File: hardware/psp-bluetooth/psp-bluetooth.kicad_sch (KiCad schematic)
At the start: 16 parts, among them J1 Left Connector, J2 Center Connector, J3 Right Connector, J4 Analog Connector, J5 PSP Power out, J6 Power IN, J7 Serial, J8 Vin Toggle, P1 Digital, P2 Analog, P3 CONN_01X01, P4 CONN_01X01, P5 CONN_01X01, P6 CONN_01X01, U1 MCP4251-xxxx-P

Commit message: Final
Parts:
- removed J6: Power IN, Connector_PinHeader_2.54mm:PinHeader_1x02_P2.54mm_Vertical, symbol Connector_Generic:Conn_01x02
- added J6: Barrel_Jack, Connector_BarrelJack:BarrelJack_CUI_PJ-063AH_Horizontal, symbol Connector:Barrel_Jack
- added JP1: SJ Vin Toggle, Jumper:SolderJumper-2_P1.3mm_Open_Pad1.0x1.5mm, symbol Jumper:SolderJumper_2_Open
- added SW1: SW_Push, Button_Switch_SMD:SW_Push_1P1T_NO_6x6mm_H9.5mm, symbol Switch:SW_Push
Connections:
- net 10(**/SS): no longer U1.1 (~{CS})
- net 11(**/MOSI): no longer U1.3 (SDI)
- net A6 (D20): now also SW1.1
- net GND: now also J6.1, SW1.2
- net VIN: now also JP1.2 (B)
- net P1W: now reaches J4.2 (Pin_2), U1.6 (P1W)
- net P0A/P1A: now reaches J4.3 (Pin_3), U1.7 (P1A), U1.8 (P0A)
- net P0W: now reaches J4.4 (Pin_4), U1.9 (P0W)
- net at J5.2 (Pin_2), J8.1 (Pin_1), S1.2: now also JP1.1 (A)
- net at S1.3: now also J6.2
- new net 10(**/SS): U1.1 (~{CS})
- new net 11(**/MOSI): U1.3 (SDI)
- no-connect marks 18 -> 17
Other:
- moved on the sheet: J7

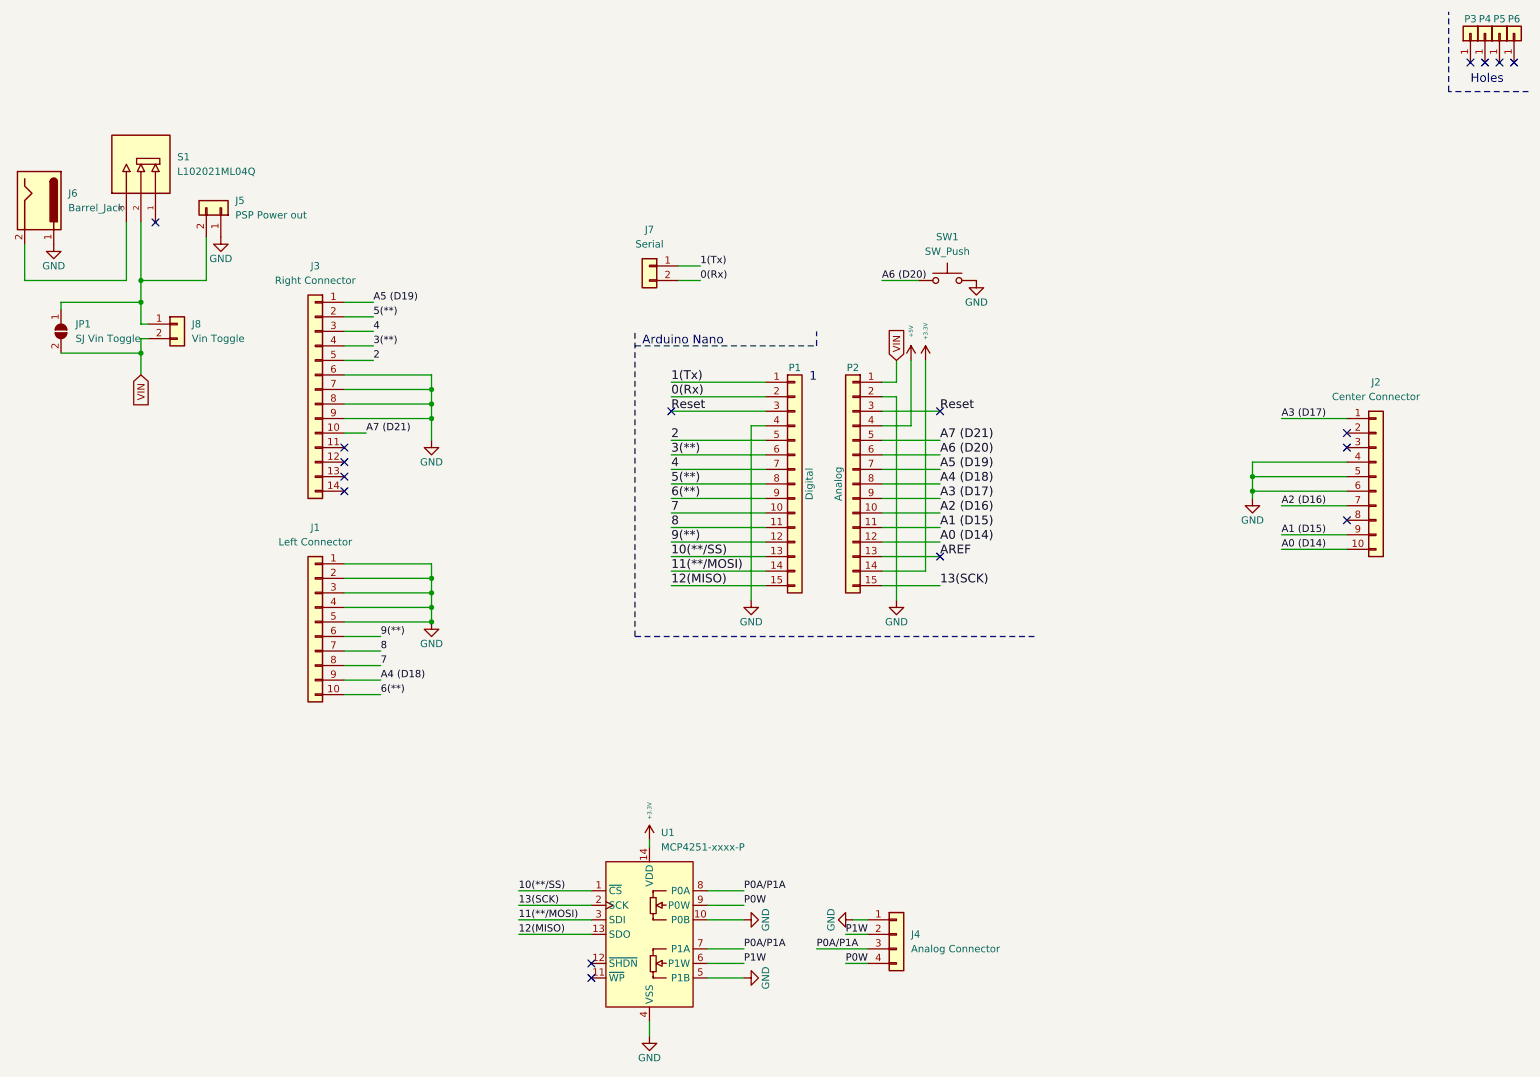
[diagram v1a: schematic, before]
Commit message: Made kicad project portable and finished V1.
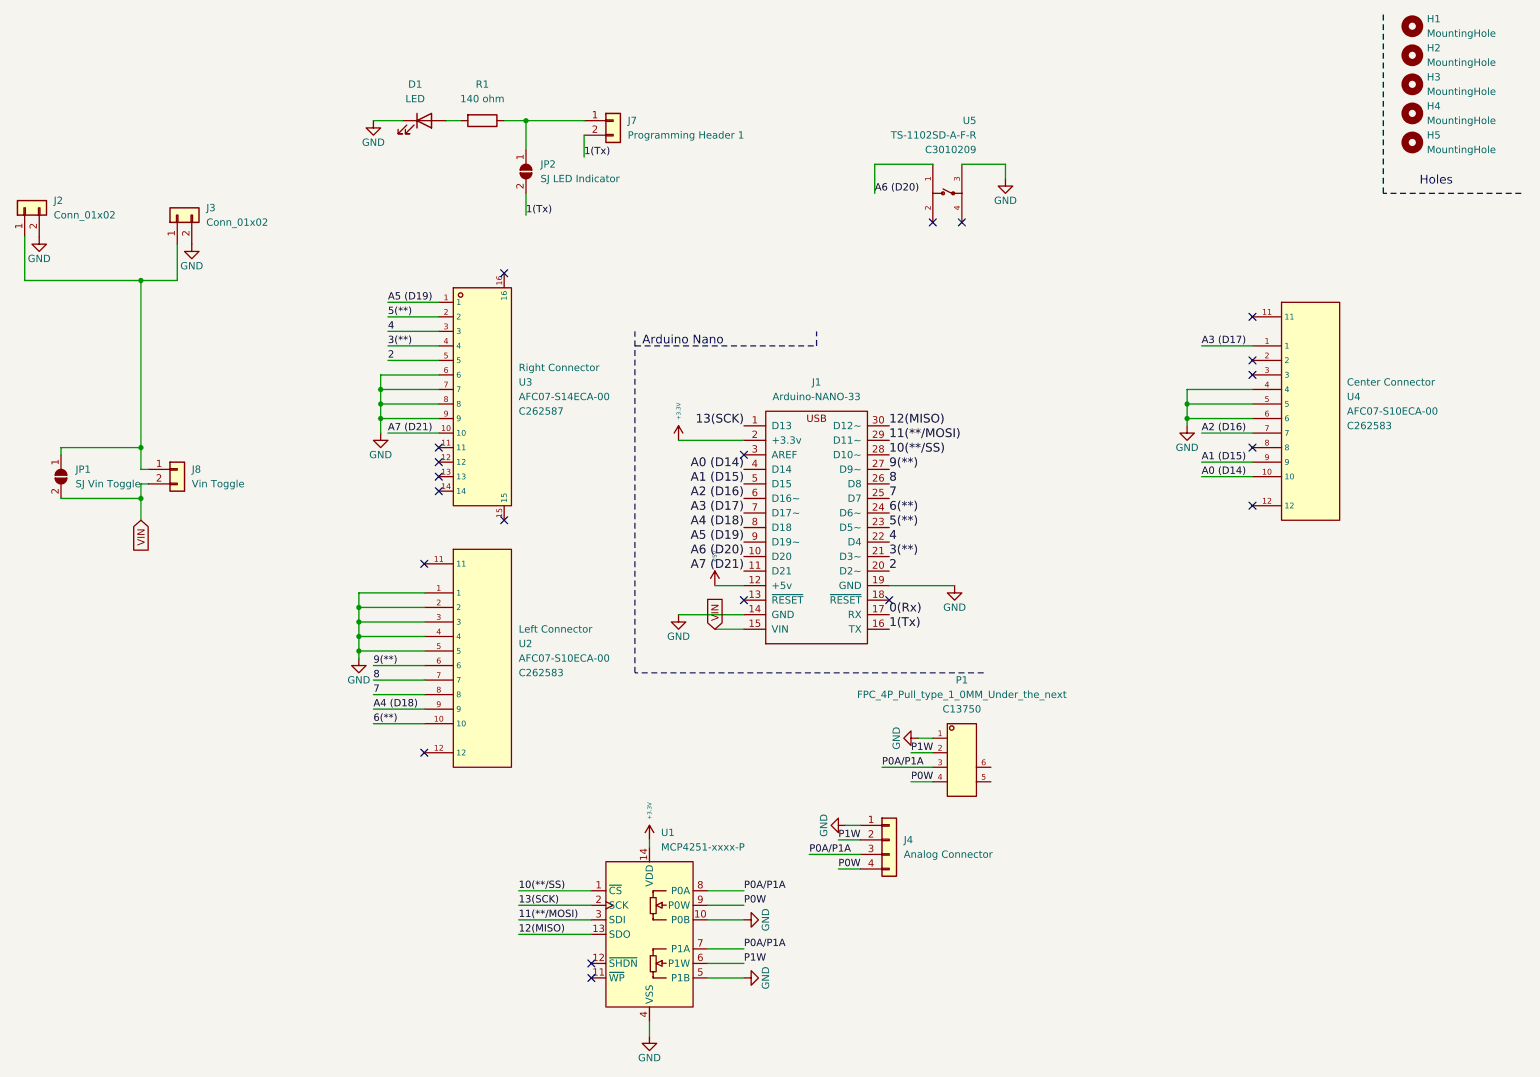
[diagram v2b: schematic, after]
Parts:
- removed J1: Left Connector, Connector_FFC-FPC:Hirose_FH12-10S-0.5SH_1x10-1MP_P0.50mm_Horizontal, symbol Connector_Generic:Conn_01x10
- removed J2: Center Connector, Connector_FFC-FPC:Hirose_FH12-10S-0.5SH_1x10-1MP_P0.50mm_Horizontal, symbol Connector_Generic:Conn_01x10
- removed J3: Right Connector, Connector_FFC-FPC:Hirose_FH12-14S-0.5SH_1x14-1MP_P0.50mm_Horizontal, symbol Connector_Generic:Conn_01x14
- removed J5: PSP Power out, Connector_PinHeader_2.54mm:PinHeader_1x02_P2.54mm_Vertical, symbol Connector_Generic:Conn_01x02
- removed J6: Barrel_Jack, Connector_BarrelJack:BarrelJack_CUI_PJ-063AH_Horizontal, symbol Connector:Barrel_Jack
- removed P1: Digital, Socket_Arduino_Nano:Socket_Strip_Arduino_1x15, symbol Connector_Generic:Conn_01x15
- removed P2: Analog, Socket_Arduino_Nano:Socket_Strip_Arduino_1x15, symbol Connector_Generic:Conn_01x15
- removed P3, P4, P5, P6: CONN_01X01, Socket_Arduino_Nano:1pin_Nano, symbol Connector_Generic:Conn_01x01
- removed S1: L102021ML04Q, L102021ML04Q:SW_L102021ML04Q, symbol L102021ML04Q:L102021ML04Q
- removed SW1: SW_Push, Button_Switch_SMD:SW_Push_1P1T_NO_6x6mm_H9.5mm, symbol Switch:SW_Push
- added D1: LED, LED_THT:LED_D3.0mm_Horizontal_O1.27mm_Z6.0mm, symbol Device:LED
- added H1, H2, H3, H4, H5: MountingHole, MountingHole:MountingHole_2.5mm, symbol Mechanical:MountingHole
- added J1: Arduino-NANO-33, Nano_33:NANO_33_Socket_Castell&SMD, symbol Arduino-nano-33:Arduino-NANO-33
- added J2, J3: Conn_01x02, Connector_PinHeader_2.54mm:PinHeader_1x02_P2.54mm_Vertical, symbol Connector_Generic:Conn_01x02
- added JP2: SJ LED Indicator, Jumper:SolderJumper-2_P1.3mm_Open_Pad1.0x1.5mm, symbol Jumper:SolderJumper_2_Open
- added P1: FPC_4P_Pull_type_1_0MM_Under_the_next, JLCPCB_footprint:FPC-SMD_AFA07-S04FCC-00, symbol JLCPCB_schematic:FPC_4P_Pull_type_1_0MM_Under_the_next
- added R1: 140 ohm, Resistor_THT:R_Axial_DIN0207_L6.3mm_D2.5mm_P10.16mm_Horizontal, symbol Device:R
- added U2, U4: AFC07-S10ECA-00, JLCPCB_footprint:FPC-SMD_P0.50-10P_LCS-SJ-H2.0, symbol JLCPCB_schematic:AFC07-S10ECA-00
- added U3: AFC07-S14ECA-00, JLCPCB_footprint:FPC-SMD_P0.50-14P_LCS-SJ-H2.0, symbol JLCPCB_schematic:AFC07-S14ECA-00
- added U5: TS-1102SD-A-F-R, JLCPCB_footprint:SW-SMD_4P-L6.0-W6.0-P4.50-LS9.2, symbol JLCPCB_schematic:TS-1102SD-A-F-R
- J7: value Serial -> Programming Header 1
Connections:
- net +3V3: now also J1.2 (+3.3v)
- net +5V: now also J1.12 (+5v)
- net 0(Rx): now also J1.17 (RX); no longer J7.2 (Pin_2)
- net 1(Tx): now also J7.2 (Pin_2), J1.16 (TX), JP2.2 (B); no longer J7.1 (Pin_1)
- net 10(**/SS): now also J1.28 (D10~)
- net 11(**/MOSI): now also J1.29 (D11~)
- net 12(MISO): now also J1.30 (D12~)
- net 13(SCK): now also J1.1 (D13)
- net 2: now also J1.20 (D2~), U3.5
- net 3(**): now also J1.21 (D3~), U3.4
- net 4: now also J1.22 (D4), U3.3
- net 5(**): now also J1.23 (D5~), U3.2
- net 6(**): now also J1.24 (D6~), U2.10
- net 7: now also J1.25 (D7), U2.8
- net 8: now also J1.26 (D8), U2.7
- net 9(**): now also J1.27 (D9~), U2.6
- net A0 (D14): now also J1.4 (D14), U4.10
- net A1 (D15): now also J1.5 (D15), U4.9
- net A2 (D16): now also J1.6 (D16~), U4.7
- net A3 (D17): now also J1.7 (D17~), U4.1
- net A4 (D18): now also J1.8 (D18), U2.9
- net A5 (D19): now also J1.9 (D19~), U3.1
- net A6 (D20): now also J1.10 (D20), U5.1
- net A7 (D21): now also J1.11 (D21), U3.10
- net GND: now also D1.1 (K), J1.14 (GND), J1.19 (GND), J2.2 (Pin_2), J3.2 (Pin_2), P1.1, U2.1, U2.2, U2.3, U2.4, U2.5, U3.6, U3.7, U3.8, U3.9, U4.4, U4.5, U4.6, U5.3
- net P0A/P1A: now also P1.3
- net P0W: now also P1.4
- net P1W: now also P1.2
- net VIN: now also J1.15 (VIN)
- net at J8.1 (Pin_1), JP1.1 (A): now also J2.1 (Pin_1), J3.1 (Pin_1)
- new net: D1.2 (A), R1.2
- new net: J7.1 (Pin_1), JP2.1 (A), R1.1
- no-connect marks 17 -> 20
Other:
- note removed: "1"
- company: (none) -> https://github.com/ste2425/PSP-Consolizer
- title: (none) -> PSP Consolizer Board
- moved on the sheet: J4, J8, JP1
